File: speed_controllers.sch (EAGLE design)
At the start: 9 parts

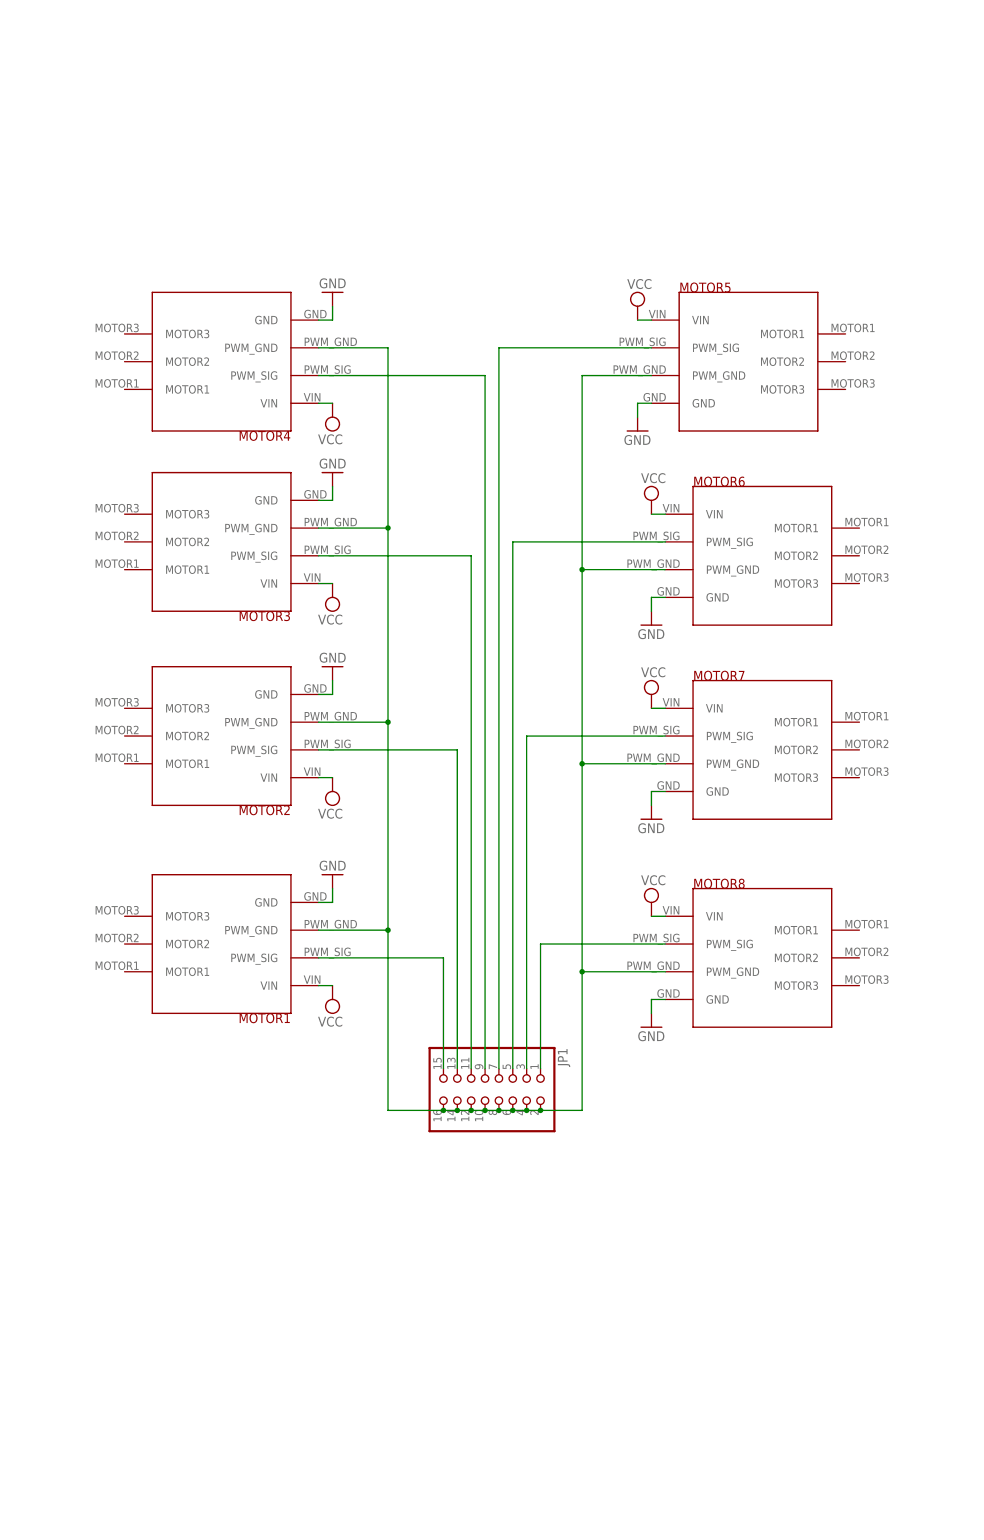
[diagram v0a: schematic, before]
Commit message: Added MOSFETs to speed controllers
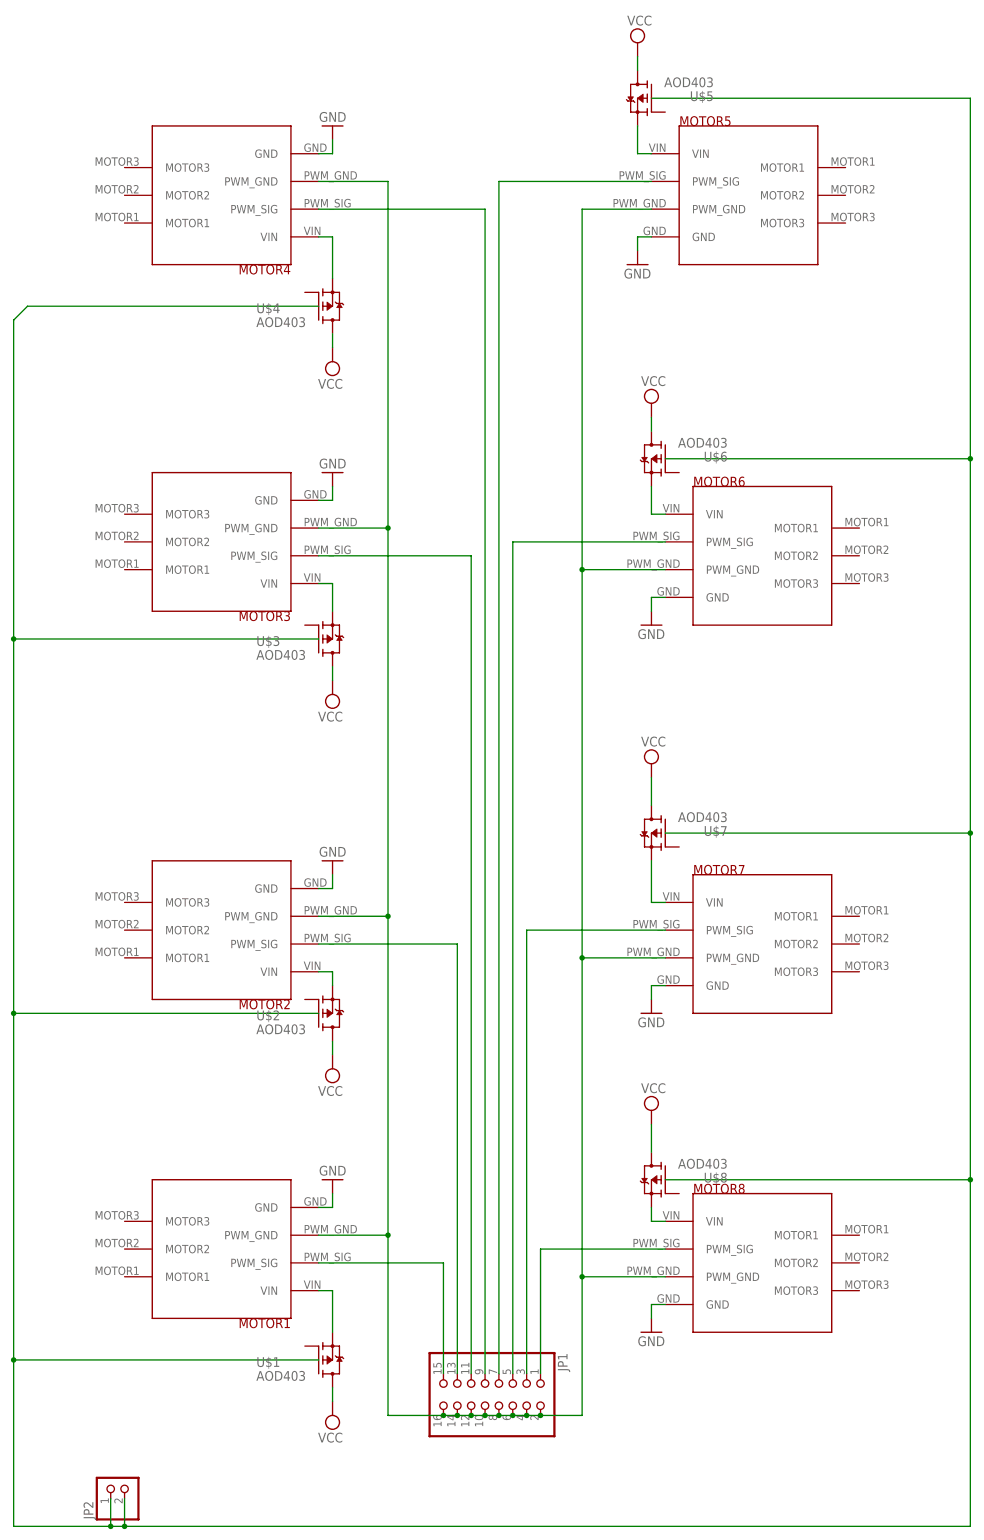
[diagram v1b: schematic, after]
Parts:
- added JP2: (no value), auv:PINHD-1X2
- added U$1, U$2, U$3, U$4, U$5, U$6, U$7, U$8: AOD403, auv:AOD403
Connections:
- new net N$10: MOTOR1.VIN, U$1.S
- new net N$11: MOTOR2.VIN, U$2.S
- new net N$12: MOTOR3.VIN, U$3.S
- new net N$13: MOTOR4.VIN, U$4.S
- new net N$14: MOTOR7.VIN, U$7.S
- new net N$15: MOTOR6.VIN, U$6.S
- new net N$16: MOTOR8.VIN, U$8.S
- new net N$17: JP2.1, JP2.2
- new net N$19: MOTOR5.VIN, U$5.S
- net VCC: now also U$1.D, U$2.D, U$3.D, U$4.D, U$5.D, U$6.D, U$7.D, U$8.D; no longer MOTOR1.VIN, MOTOR2.VIN, MOTOR3.VIN, MOTOR4.VIN, MOTOR5.VIN, MOTOR6.VIN, MOTOR7.VIN, MOTOR8.VIN
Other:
- moved on the sheet: JP1, MOTOR1, MOTOR2, MOTOR4, MOTOR5, MOTOR7, MOTOR8
